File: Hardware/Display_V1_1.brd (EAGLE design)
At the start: 96 x 82 mm, 91 parts, among them IC1 STM32F030C6T, IC2 LM2623, IC3 MCP73831, IC4 LP2985M5, M1 WIRELESS-NRF24L01, Q1 BSS138, Q10 BSS138, Q11 IRLML5203, Q12 BSS138, Q13 IRLML5203, Q14 BSS138, Q15 IRLML5203, Q16 BSS138, Q17 IRLML5203, Q18 BC817-16LT1SMD, Q19 BC817-16LT1SMD, Q2 BSS138, Q3 BSS138, Q4 BSS138, Q5 BSS138, Q6 BSS138, Q7 BSS138, Q8 BSS138, Q9 IRLML5203, X1 MINI-USB-UX60-MB-5ST, Y1 8MHz

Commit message: last(?) changes
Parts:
- D2: device diode:SOD323-W -> diode:MINIMELF
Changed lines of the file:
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@@
 <attribute name="VALUE" x="80.9625" y="64.77" size="1.27" layer="27" rot="R180"/>
 </element>
-<element name="D2" library="diode" package="SOD323-W" value="1N4148" x="83.185" y="66.04" smashed="yes" rot="R270">
+<element name="D2" library="diode" package="MINIMELF" value="1N4148" x="83.185" y="66.04" smashed="yes" rot="R270">
 <attribute name="NAME" x="83.7725" y="61.765" size="1.016" layer="25" font="vector" rot="R90"/>
 <attribute name="VALUE" x="80.885" y="67.14" size="1.27" layer="27" rot="R270"/>
@@
 <wire x1="80.3775" y1="65.405" x2="83.185" y2="65.405" width="0.3048" layer="1"/>
 <wire x1="83.185" y1="65.405" x2="87.4825" y2="65.405" width="0.3048" layer="1"/>
-<wire x1="83.185" y1="64.59" x2="83.185" y2="65.405" width="0.3048" layer="1"/>
+<wire x1="83.185" y1="64.34" x2="83.185" y2="65.405" width="0.3048" layer="1"/>
 </signal>
 <signal name="/DISABLE">
@@
 <contactref element="S4" pad="2"/>
 <wire x1="81.7394" y1="71.2446" x2="83.185" y2="69.799" width="0.4064" layer="1"/>
-<wire x1="83.185" y1="69.799" x2="83.185" y2="67.49" width="0.4064" layer="1"/>
-<wire x1="83.185" y1="67.49" x2="82.4125" y2="67.49" width="0.4064" layer="1"/>
-<wire x1="82.4125" y1="67.49" x2="81.915" y2="66.9925" width="0.4064" layer="1"/>
-<via x="81.915" y="66.9925" extent="1-16" drill="0.3048" shape="octagon"/>
-<wire x1="81.915" y1="66.9925" x2="81.915" y2="63.8175" width="0.4064" layer="16"/>
-<wire x1="81.915" y1="63.8175" x2="82.8675" y2="62.865" width="0.4064" layer="16"/>
+<wire x1="83.185" y1="69.799" x2="83.185" y2="67.74" width="0.4064" layer="1"/>
+<via x="81.5975" y="66.9925" extent="1-16" drill="0.3048" shape="octagon"/>
+<wire x1="81.5975" y1="66.9925" x2="81.5975" y2="64.135" width="0.4064" layer="16"/>
+<wire x1="81.5975" y1="64.135" x2="82.8675" y2="62.865" width="0.4064" layer="16"/>
 <via x="82.8675" y="62.865" extent="1-16" drill="0.3048" shape="octagon"/>
 <wire x1="82.8675" y1="62.865" x2="82.8675" y2="46.0375" width="0.4064" layer="1"/>
@@
 <wire x1="57.4675" y1="41.91" x2="78.74" y2="41.91" width="0.4064" layer="1"/>
 <wire x1="78.74" y1="41.91" x2="82.8675" y2="46.0375" width="0.4064" layer="1"/>
+<wire x1="81.5975" y1="66.9925" x2="82.345" y2="67.74" width="0.4064" layer="1"/>
+<wire x1="82.345" y1="67.74" x2="83.185" y2="67.74" width="0.4064" layer="1"/>
 </signal>
 <signal name="N$28">

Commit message: Final PCB changes
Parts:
- IC2: value LM2623 -> LM2623MM; device v-reg-3:SO08 -> v-reg-3:MSOP08
- R1: value 150 -> 120
- moved LED 9.84 mm to (42.9, 6.99), turned to 270 degrees
- moved PAD1 6.04 mm to (74.0, 15.2)
- moved PAD2 6.04 mm to (74.0, 61.6)
- moved R16 1.90 mm to (47.9, 7.30), turned to 0 degrees
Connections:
- net N$16 renamed V+
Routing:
- net VIN: track 15.2 -> 23.1 mm
- net N$22: track 1.39 -> 3.61 mm
- net N$26: track 6.56 -> 7.69 mm
- net COM2: track 110.5 -> 111.6 mm
- net N$23: track 19.2 -> 19.7 mm

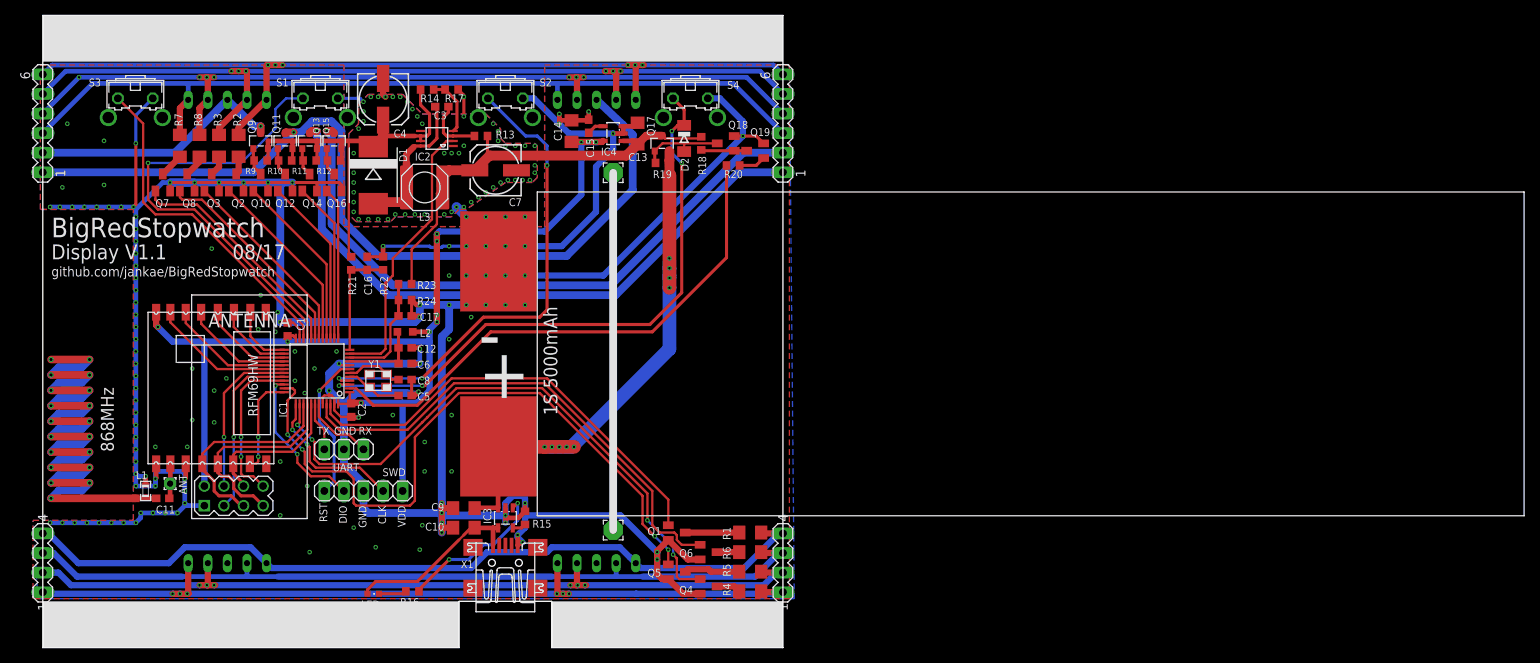
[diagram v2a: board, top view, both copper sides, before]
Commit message: Slight changes for easier fabrication
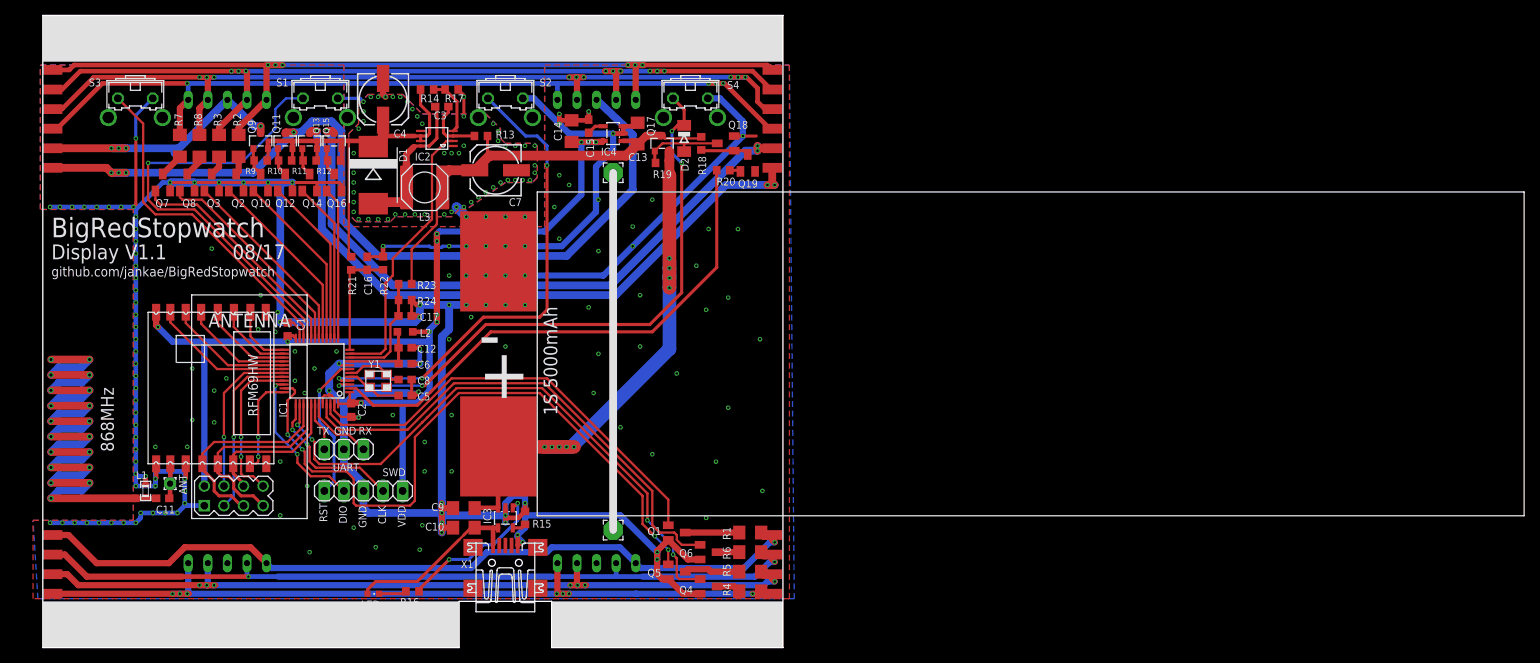
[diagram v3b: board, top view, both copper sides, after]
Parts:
- removed IN1, OUT1: (no value), con-lstb:MA04-1
- removed IN2, OUT2: (no value), con-lstb:MA06-1
- added PAD10, PAD11, PAD12, PAD13, PAD14, PAD15, PAD16, PAD17, PAD18, PAD19, PAD20, PAD21, PAD22, PAD3, PAD4, PAD5, PAD6, PAD7, PAD8, PAD9: (no value), wirepad:SMD1,27-2,54
- moved Q19 1.85 mm to (91.4, 62.9), turned to 0 degrees
- moved R20 1.42 mm to (88.3, 61.9)
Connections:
- net COM1: now also PAD15.1; no longer IN2.2
- net COM2: now also PAD16.1; no longer IN2.1
- net COM3: now also PAD21.1; no longer OUT2.2
- net COM4: now also PAD22.1; no longer OUT2.1
- net DP: now also PAD3.1, PAD7.1; no longer IN1.4, OUT1.4
- net SEG_A: now also PAD13.1, PAD19.1; no longer IN2.4, OUT2.4
- net SEG_B: now also PAD14.1, PAD20.1; no longer IN2.3, OUT2.3
- net SEG_C: now also PAD4.1, PAD8.1; no longer IN1.3, OUT1.3
- net SEG_D: now also PAD5.1, PAD9.1; no longer IN1.2, OUT1.2
- net SEG_E: now also PAD10.1, PAD6.1; no longer IN1.1, OUT1.1
- net SEG_F: now also PAD12.1, PAD18.1; no longer IN2.5, OUT2.5
- net SEG_G: now also PAD11.1, PAD17.1; no longer IN2.6, OUT2.6
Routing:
- net SEG_E: track 110.8 -> 106.8 mm, vias 6 -> 7
- net SEG_G: track 120.2 -> 117.0 mm
- net SEG_C: track 105.0 -> 101.9 mm, vias 0 -> 2
- net DP: track 106.5 -> 103.4 mm, vias 0 -> 1
- net SEG_D: track 110.1 -> 107.1 mm, vias 6 -> 7
- net N$28: track 3.50 -> 1.52 mm
- net COM4: track 84.0 -> 85.4 mm, vias 1 -> 3
- net SEG_F: track 116.2 -> 114.9 mm, vias 6 -> 9
- net GND: track 552.4 -> 551.1 mm, vias 193 -> 217
- net DISABLE: track 69.7 -> 68.5 mm
- net COM2: track 111.6 -> 112.5 mm, vias 1 -> 4
- net COM1: track 33.4 -> 33.9 mm, vias 1 -> 4
- net SEG_B: track 110.7 -> 110.4 mm, vias 0 -> 4
- net SEG_A: track 114.6 -> 114.4 mm, vias 7 -> 9
- net COM3: vias 1 -> 3

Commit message: Bugfixes and improvements, basic system working
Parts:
- R10, R11, R12, R9: value 100k -> 3k3
- R4: value 68 -> 120
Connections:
- removed net DOT: IC1.46, Q1.1
- new net S_DOT: IC1.38, Q4.1
- net DP: now also PAD10.1, PAD6.1, R4.2, SEG1.1, SEG2.1; no longer PAD3.1, PAD7.1, R1.2, SEG1.5, SEG2.5
- net SEG_C: now also PAD5.1, PAD9.1, R5.2, SEG1.2, SEG2.2; no longer PAD4.1, PAD8.1, R6.2, SEG1.4, SEG2.4
- net SEG_D: now also PAD4.1, PAD8.1, R6.2, SEG1.4, SEG2.4; no longer PAD5.1, PAD9.1, R5.2, SEG1.2, SEG2.2
- net SEG_E: now also PAD3.1, PAD7.1, R1.2, SEG1.5, SEG2.5; no longer PAD10.1, PAD6.1, R4.2, SEG1.1, SEG2.1
- net S_C: now also IC1.35, Q5.1; no longer IC1.45, Q6.1
- net S_D: now also IC1.45, Q6.1; no longer IC1.35, Q5.1
- net S_E: now also IC1.46, Q1.1; no longer IC1.38, Q4.1
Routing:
- net S_DOT: track 0.00 -> 76.9 mm, vias 0 -> 4
- net DOT: track 58.1 -> 0.00 mm
- net S_D: track 87.0 -> 65.0 mm, vias 4 -> 0
- net S_C: track 65.0 -> 87.0 mm, vias 0 -> 4
- net S_E: track 76.9 -> 58.1 mm, vias 4 -> 0
- net SEG_D: track 107.1 -> 101.9 mm, vias 7 -> 2
- net SEG_C: track 101.9 -> 107.1 mm, vias 2 -> 7
- net SEG_E: track 106.8 -> 103.4 mm, vias 7 -> 1
- net DP: track 103.4 -> 106.8 mm, vias 1 -> 7
